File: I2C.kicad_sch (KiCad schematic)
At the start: 1 part

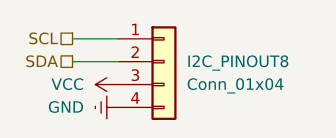
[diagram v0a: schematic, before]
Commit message: move all backside components to front and make it work for jlc basic components
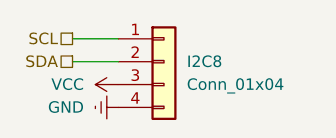
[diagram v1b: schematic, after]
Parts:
- renumbered I2C_PINOUT8 to I2C8
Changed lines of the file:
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@@
 		(dnp no)
 		(fields_autoplaced yes)
-		(property "Reference" "I2C_PINOUT8"
+		(property "Reference" "I2C8"
 			(at 162.56 85.0899 0)
 			(effects
@@
 			(project "shadow"
 				(path "/3c2fce68-ba60-4bda-a294-ddd60ff77106/1f4d8b00-c3b2-41db-a404-37456fc3406d"
-					(reference "I2C_PINOUT8")
+					(reference "I2C8")
 					(unit 1)
 				)
 				(path "/3c2fce68-ba60-4bda-a294-ddd60ff77106/2c8d79c1-e455-4de4-83e3-c8c9d3f6f47a"
-					(reference "I2C_PINOUT12")
+					(reference "I2C12")
 					(unit 1)
 				)
 				(path "/3c2fce68-ba60-4bda-a294-ddd60ff77106/33efbf78-e978-471c-9cea-15367c539204"
-					(reference "I2C_PINOUT10")
+					(reference "I2C10")
 					(unit 1)
 				)
 				(path "/3c2fce68-ba60-4bda-a294-ddd60ff77106/4142de63-05f7-4148-b67f-adf34c320d8e"
-					(reference "I2C_PINOUT11")
+					(reference "I2C11")
 					(unit 1)
 				)
 				(path "/3c2fce68-ba60-4bda-a294-ddd60ff77106/5312e096-6ef0-46e5-b6b9-965bc5c9d2e1"
-					(reference "I2C_PINOUT1")
+					(reference "I2C1")
 					(unit 1)
 				)
 				(path "/3c2fce68-ba60-4bda-a294-ddd60ff77106/642870dc-8a2b-449d-80d8-12a116942eb6"
-					(reference "I2C_PINOUT6")
+					(reference "I2C6")
 					(unit 1)
 				)
 				(path "/3c2fce68-ba60-4bda-a294-ddd60ff77106/6d11c068-6d98-437f-8725-9d48a876a04d"
-					(reference "I2C_PINOUT0")
+					(reference "I2C0")
 					(unit 1)
 				)
 				(path "/3c2fce68-ba60-4bda-a294-ddd60ff77106/80e3d8a1-7962-4df6-b6f8-c25855f05fe1"
-					(reference "I2C_PINOUT9")
+					(reference "I2C9")
 					(unit 1)
 				)
 				(path "/3c2fce68-ba60-4bda-a294-ddd60ff77106/9079efb0-12b1-43ea-a23a-3b78f179808a"
-					(reference "I2C_PINOUT5")
+					(reference "I2C5")
 					(unit 1)
 				)
 				(path "/3c2fce68-ba60-4bda-a294-ddd60ff77106/bb7a6f2a-14f3-4545-9deb-56e401c63823"
-					(reference "I2C_PINOUT4")
+					(reference "I2C4")
 					(unit 1)
 				)
 				(path "/3c2fce68-ba60-4bda-a294-ddd60ff77106/c07a994a-219d-4064-830c-ddf1cdb92214"
-					(reference "I2C_PINOUT3")
+					(reference "I2C3")
 					(unit 1)
 				)
 				(path "/3c2fce68-ba60-4bda-a294-ddd60ff77106/c1580083-c554-4948-bcc8-f17c7f357ede"
-					(reference "I2C_PINOUT7")
+					(reference "I2C7")
 					(unit 1)
 				)
 				(path "/3c2fce68-ba60-4bda-a294-ddd60ff77106/f3aa6bec-7cb4-41cf-a783-15c456af59be"
-					(reference "I2C_PINOUT2")
+					(reference "I2C2")
 					(unit 1)
 				)
